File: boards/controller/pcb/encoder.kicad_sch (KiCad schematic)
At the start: 8 parts, among them SW7001 EC11E15204A3

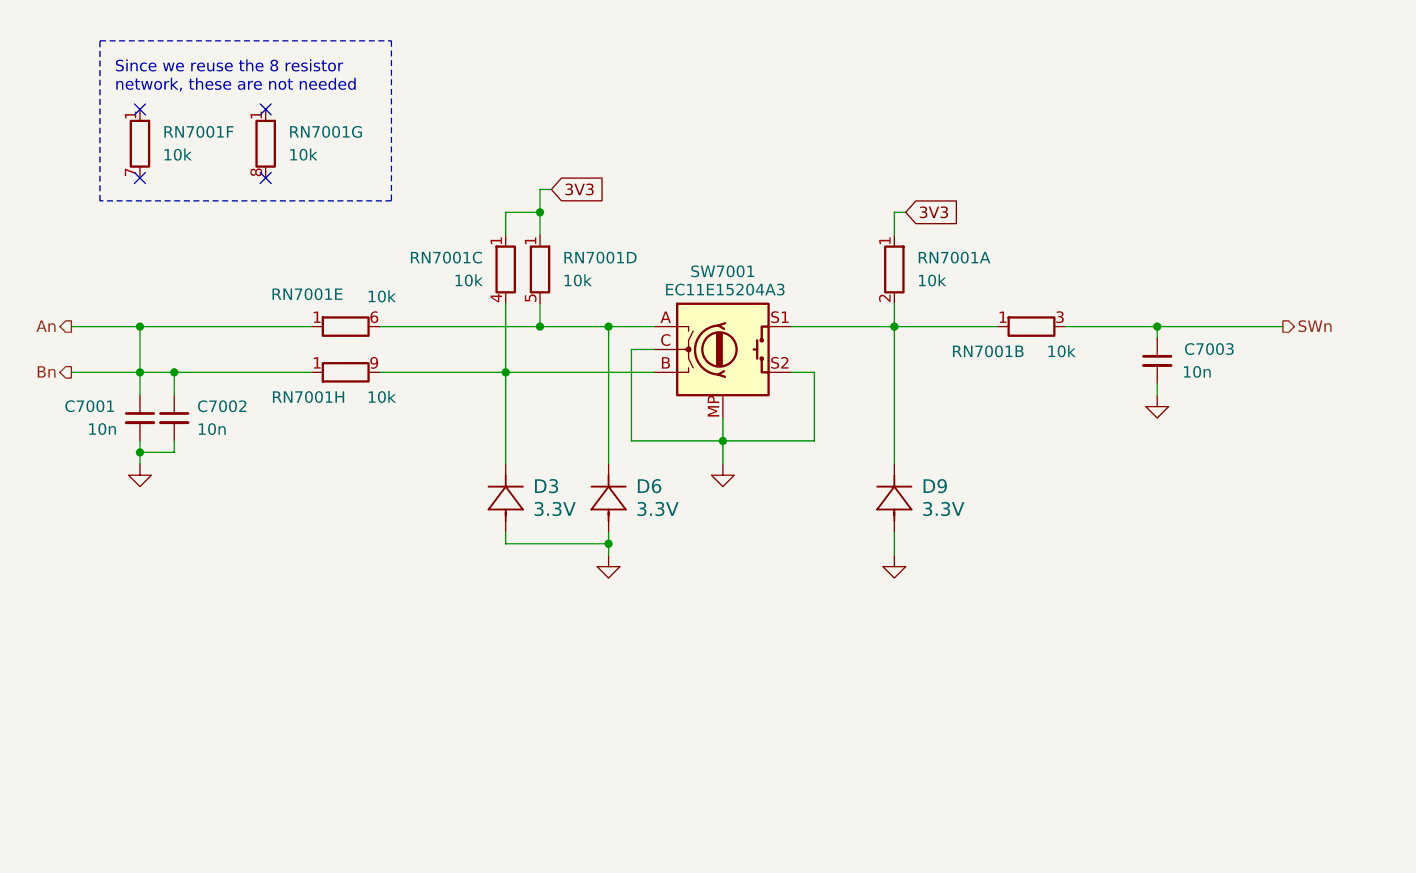
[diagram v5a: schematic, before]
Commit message: controller: pcb: Update schematic + layout
Signed-off-by: Nicholas Loehrke <nicholasnloehrke@gmail.com>
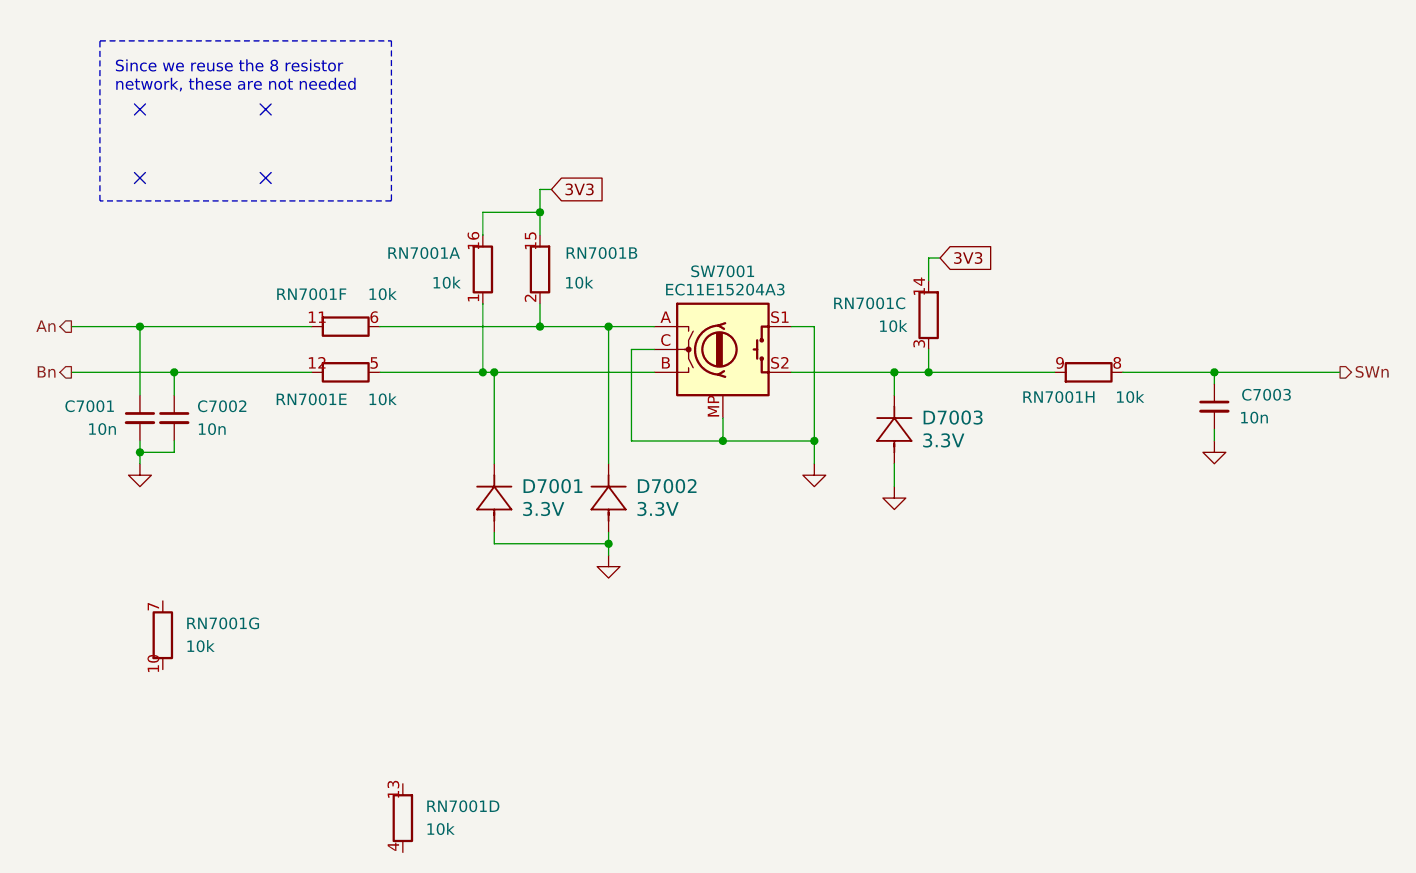
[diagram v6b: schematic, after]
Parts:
- removed RN7001: 10k, Resistor_THT:R_Array_SIP9, symbol Device:R_Network08_Split
- added RN7001: 10k, YC248-JR-0710KL:YC248-JR-0710KL, symbol Device:R_Pack08_Split
- C7001, C7002, C7003: footprint (none) -> Capacitor_SMD:C_0402_1005Metric
- D7001: renamed from D3; footprint CR_SOD-523_PNJ -> PJSD03TS-AU_R1_000A1:PJSD03TS-AU_R1_000A1
- D7002: renamed from D6; footprint CR_SOD-523_PNJ -> PJSD03TS-AU_R1_000A1:PJSD03TS-AU_R1_000A1
- D7003: renamed from D9; footprint CR_SOD-523_PNJ -> PJSD03TS-AU_R1_000A1:PJSD03TS-AU_R1_000A1
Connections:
- net 3V3: now also RN7001.14 (R3.2), RN7001.15 (R2.2), RN7001.16 (R1.2)
- net An: now also RN7001.11 (R6.2); no longer C7002.1
- net GND: now also SW7001.S1; no longer SW7001.S2
- net SWn: now also RN7001.8 (R8.1)
- net at D7002.1, SW7001.A: now also RN7001.2 (R2.1), RN7001.6 (R6.1)
- net at D7001.1, SW7001.B: now also RN7001.1 (R1.1), RN7001.5 (R5.1)
- net at D7003.1: now also SW7001.S2, RN7001.3 (R3.1), RN7001.9 (R8.2); no longer SW7001.S1
- new net Bn: C7002.1, RN7001.12 (R5.2)
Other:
- moved on the sheet: C7003, D7001, D7003

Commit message: controller: Update BOM
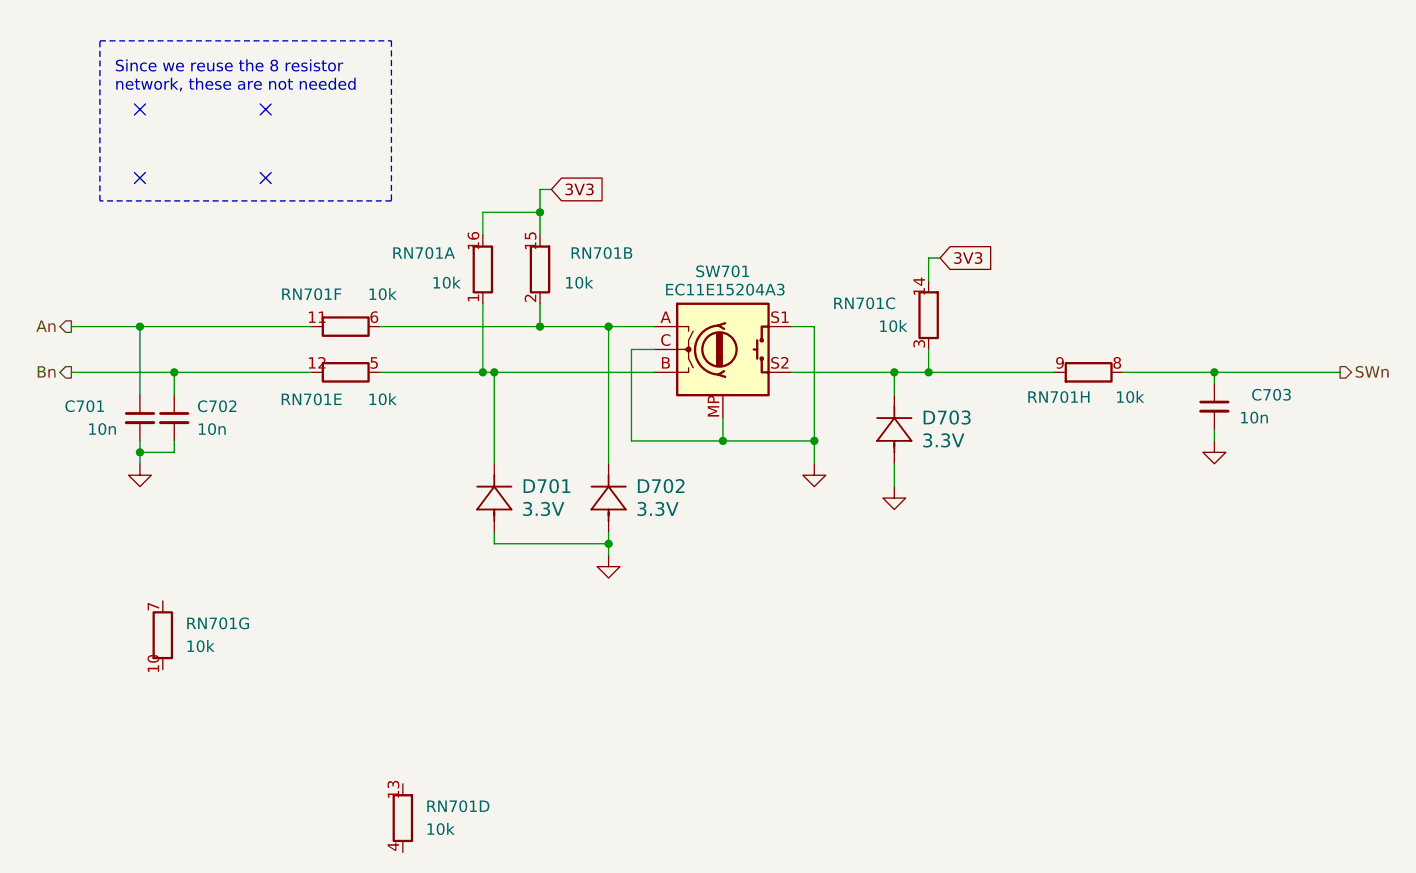
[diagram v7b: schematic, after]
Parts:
- D701: renamed from D7001; MPN (none) -> PJSD03TS-AU_R1_000A1
- D702: renamed from D7002; MPN (none) -> PJSD03TS-AU_R1_000A1
- D703: renamed from D7003; MPN (none) -> PJSD03TS-AU_R1_000A1
- RN701: renamed from RN7001; MPN (none) -> YC248-JR-0710KL
- SW701: renamed from SW7001; MPN (none) -> EC11E15204A3
- renumbered C7001 to C701, C7002 to C702, C7003 to C703
